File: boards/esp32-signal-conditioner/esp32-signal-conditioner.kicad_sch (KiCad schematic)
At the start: 0 parts

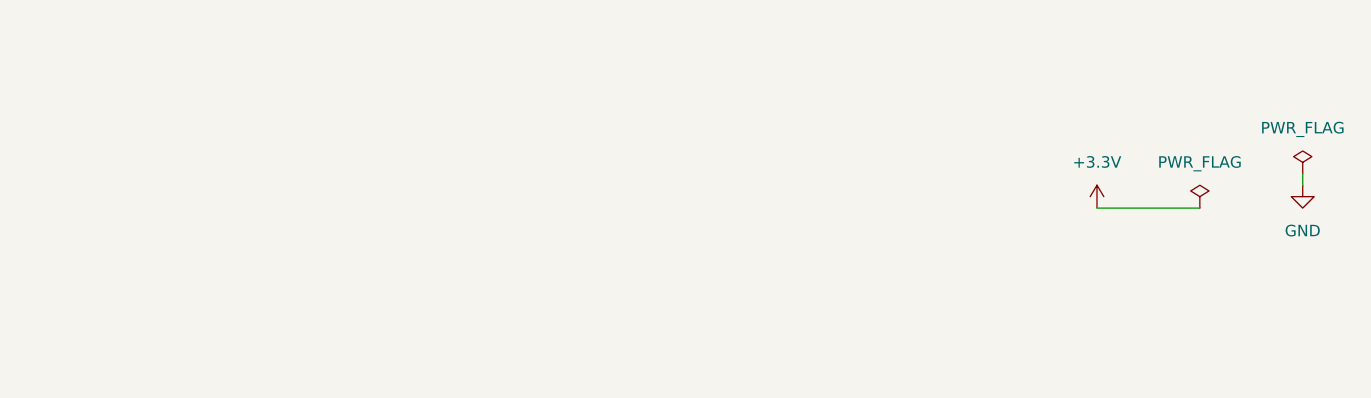
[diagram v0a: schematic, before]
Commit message: Add CH1 analog input circuit R1=11k R2=10k C1=68nF, ERC clean
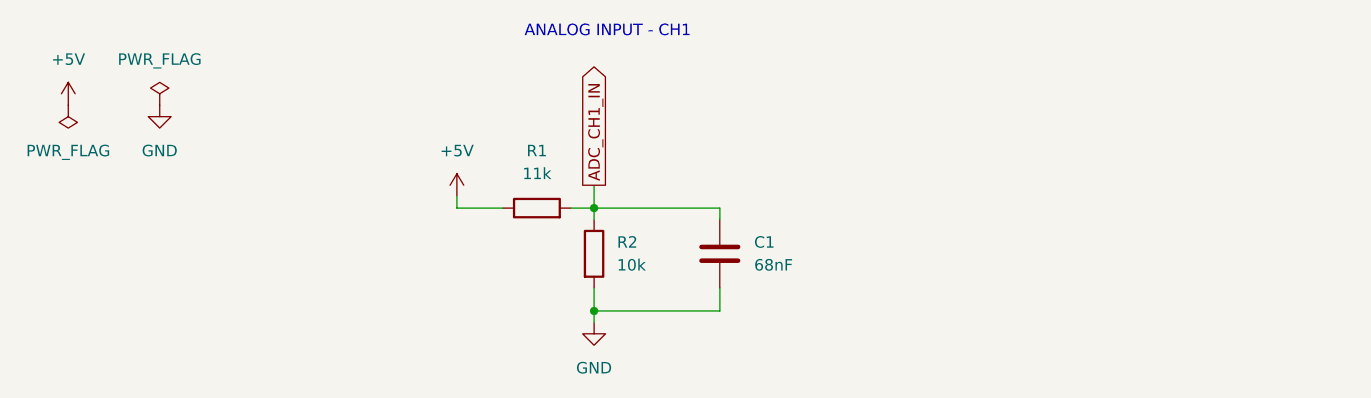
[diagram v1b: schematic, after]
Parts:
- added C1: 68nF, symbol Device:C
- added R1: 11k, symbol Device:R
- added R2: 10k, symbol Device:R
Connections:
- net GND: now also C1.2, R2.2
- new net +5V: R1.1
- new net ADC_CH1_IN: C1.1, R1.2, R2.1
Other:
- note added: "ANALOG INPUT - CH1"
